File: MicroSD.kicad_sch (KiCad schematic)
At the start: 9 parts, among them J1 Micro_SD_Card_Det1

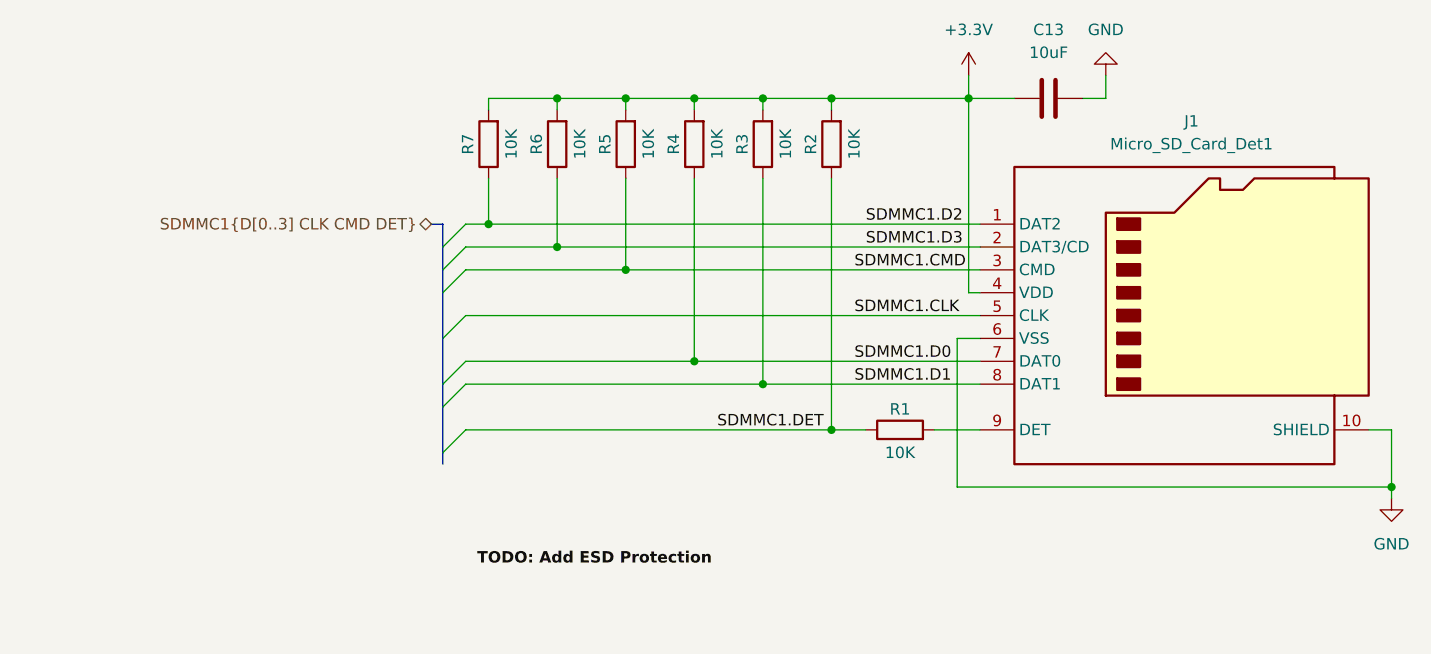
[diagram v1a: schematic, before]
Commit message: FIX : uSD Card detect
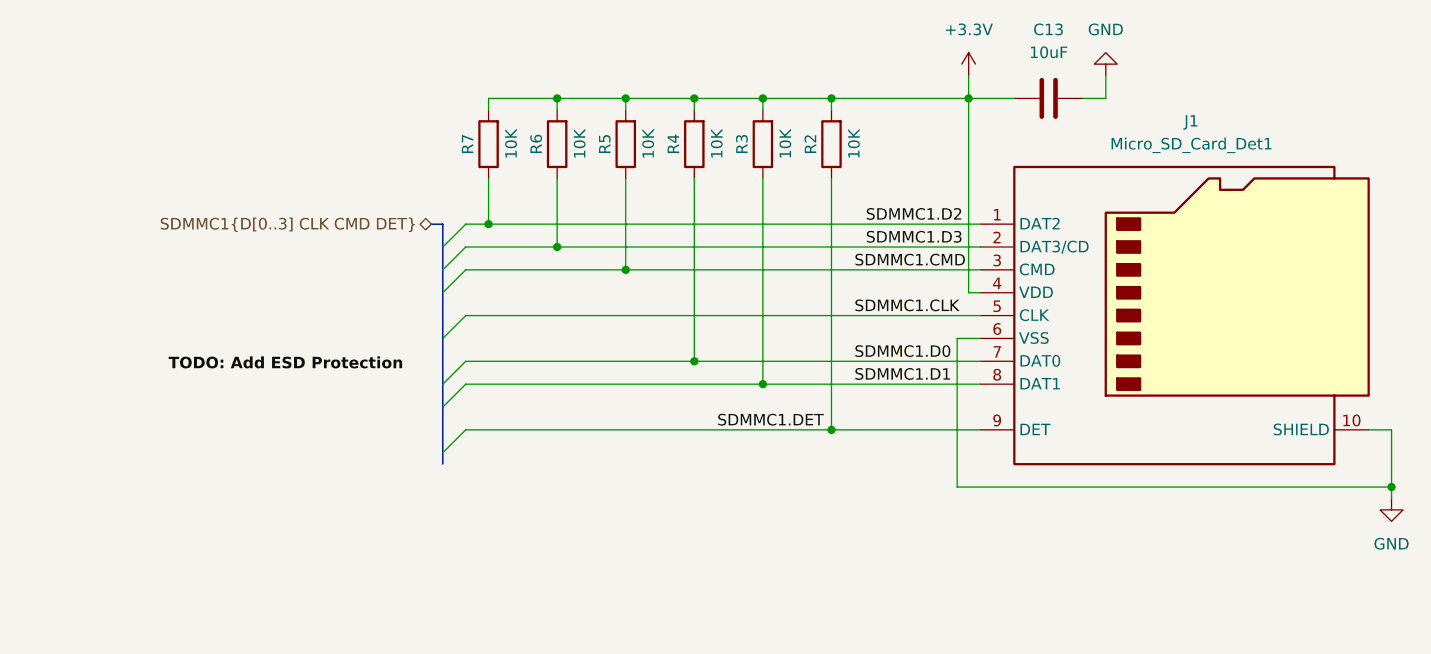
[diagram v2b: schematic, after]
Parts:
- removed R1: 10K, symbol Device:R
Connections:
- net SDMMC1.DET: now also J1.9 (DET)
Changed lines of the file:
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@@
 	(wire
 		(pts
-			(xy 105.41 109.22) (xy 109.22 109.22)
+			(xy 105.41 109.22) (xy 121.92 109.22)
 		)
 		(stroke
@@
 		(pts
 			(xy 67.31 86.36) (xy 121.92 86.36)
-		)
-		(stroke
-			(width 0)
-			(type default)
-		)
-	)
-	(wire
-		(pts
-			(xy 116.84 109.22) (xy 121.92 109.22)
 		)
 		(stroke
@@
 	)
 	(label "TODO: Add ESD Protection"
-		(at 66.04 124.46 0)
+		(at 31.75 102.87 0)
 		(effects
 			(font
@@
 					(unit 1)
 				)
-			)
-		)
-	)
-	(symbol
-		(lib_id "Device:R")
-		(at 113.03 109.22 90)
-		(unit 1)
-		(exclude_from_sim no)
-		(in_bom yes)
-		(on_board yes)
-		(dnp no)
-		(property "Reference" "R1"
-			(at 113.03 106.934 90)
-			(effects
-				(font
-					(size 1.27 1.27)
-				)
-			)
-		)
-		(property "Value" "10K"
-			(at 113.03 111.76 90)
-			(effects
-				(font
-					(size 1.27 1.27)
-				)
-			)
-		)
-		(property "Footprint" ""
-			(at 113.03 110.998 90)
-			(effects
-				(font
-					(size 1.27 1.27)
-				)
-				(hide yes)
-			)
-		)
-		(property "Datasheet" "~"
-			(at 113.03 109.22 0)
-			(effects
-				(font
-					(size 1.27 1.27)
-				)
-				(hide yes)
-			)
-		)
-		(property "Description" "Resistor"
-			(at 113.03 109.22 0)
-			(effects
-				(font
-					(size 1.27 1.27)
-				)
-				(hide yes)
-			)
-		)
-		(pin "2"
-		)
-		(pin "1"
-		)
-		(instances
-			(project "STMBlueLine"
-				(path "/d9f70aa0-fcfd-4ae4-9801-1024ce5b770a/b1a92380-38d8-44e8-bc23-33aa2ab32880"
-					(reference "R1")
-					(unit 1)
-				)

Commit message: ADD : ESD protection for uSD. FIX : uSD pullups
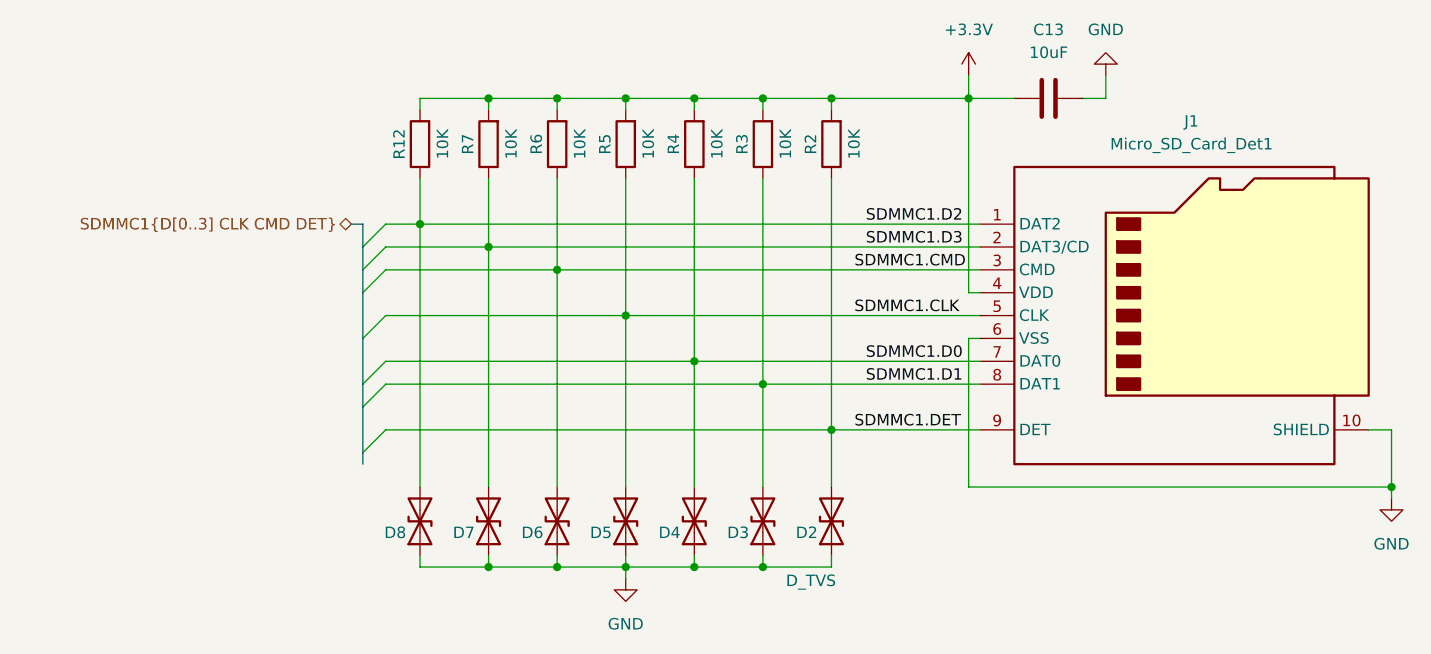
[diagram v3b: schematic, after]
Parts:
- added D2, D3, D4, D5, D6, D7, D8: D_TVS, symbol Device:D_TVS
- added R12: 10K, symbol Device:R
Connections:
- net +3.3V: now also R12.2
- net GND: now also D2.1 (A1), D3.1 (A1), D4.1 (A1), D5.1 (A1), D6.1 (A1), D7.1 (A1), D8.1 (A1)
- net SDMMC1.CLK: now also R5.1, D5.2 (A2)
- net SDMMC1.CMD: now also R6.1, D6.2 (A2); no longer R5.1
- net SDMMC1.D0: now also D4.2 (A2)
- net SDMMC1.D1: now also D3.2 (A2)
- net SDMMC1.D2: now also D8.2 (A2), R12.1; no longer R7.1
- net SDMMC1.D3: now also R7.1, D7.2 (A2); no longer R6.1
- net SDMMC1.DET: now also D2.2 (A2)

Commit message: ADD : Footprint assignment. FIX : Various ERC rules.
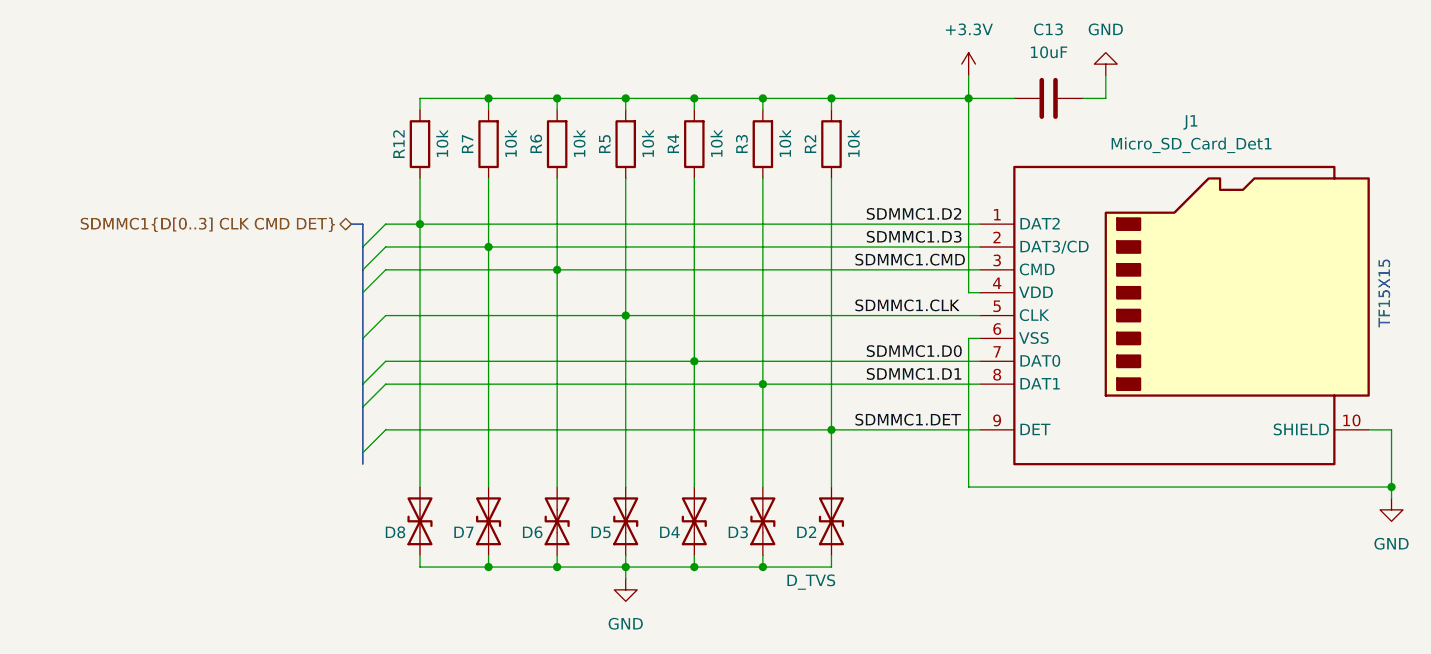
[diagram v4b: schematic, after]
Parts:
- C13: footprint (none) -> Capacitor_SMD:C_0402_1005Metric
- D2, D3, D4, D5, D6, D7, D8: footprint (none) -> Diode_SMD:D_0402_1005Metric
- J1: footprint (none) -> random-footprints:TF15X15
- R12, R2, R3, R4, R5, R6, R7: value 10K -> 10k; footprint (none) -> Resistor_SMD:R_0402_1005Metric
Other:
- note added: "TF15X15"
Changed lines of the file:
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@@
 	(generator_version "9.0")
 	(paper "A4")
+	(text "TF15X15"
+		(exclude_from_sim no)
+		(at 166.878 94.234 90)
+		(effects
+			(font
+				(size 1.27 1.27)
+			)
+		)
+	)
 	(junction
 		(at 97.79 124.46)
@@
 			)
 		)
-		(property "Value" "10K"
+		(property "Value" "10k"
 			(at 77.47 77.47 90)
 			(effects
@@
 			)
 		)
-		(property "Footprint" ""
+		(property "Footprint" "Resistor_SMD:R_0402_1005Metric"
 			(at 76.708 77.47 90)
 			(effects
@@
 			)
 		)
-		(property "Value" "10K"
+		(property "Value" "10k"
 			(at 85.09 77.47 90)
 			(effects
@@
 			)
 		)
-		(property "Footprint" ""
+		(property "Footprint" "Resistor_SMD:R_0402_1005Metric"
 			(at 84.328 77.47 90)
 			(effects
@@
 			)
 		)
-		(property "Value" "10K"
+		(property "Value" "10k"
 			(at 62.23 77.47 90)
 			(effects
@@
 			)
 		)
-		(property "Footprint" ""
+		(property "Footprint" "Resistor_SMD:R_0402_1005Metric"
 			(at 61.468 77.47 90)
 			(effects
@@
 			)
 		)
-		(property "Footprint" ""
+		(property "Footprint" "random-footprints:TF15X15"
 			(at 196.85 78.74 0)
 			(effects
@@
 			)
 		)
-		(property "Footprint" ""
+		(property "Footprint" "Diode_SMD:D_0402_1005Metric"
 			(at 105.41 119.38 0)
 			(effects
@@
 			)
 		)
-		(property "Value" "10K"
+		(property "Value" "10k"
 			(at 107.95 77.47 90)
 			(effects
@@
 			)
 		)
-		(property "Footprint" ""
+		(property "Footprint" "Resistor_SMD:R_0402_1005Metric"
 			(at 107.188 77.47 90)
 			(effects
@@
 			)
 		)
-		(property "Value" "10K"
+		(property "Value" "10k"
 			(at 69.85 77.47 90)
 			(effects
@@
 			)
 		)
-		(property "Footprint" ""
+		(property "Footprint" "Resistor_SMD:R_0402_1005Metric"
 			(at 69.088 77.47 90)
 			(effects
@@
 			)
 		)
-		(property "Footprint" ""
+		(property "Footprint" "Diode_SMD:D_0402_1005Metric"
 			(at 90.17 119.38 0)
 			(effects
@@
 			)
 		)
-		(property "Footprint" ""
+		(property "Footprint" "Diode_SMD:D_0402_1005Metric"
 			(at 59.69 119.38 0)
 			(effects
@@
 			)
 		)
-		(property "Footprint" ""
+		(property "Footprint" "Diode_SMD:D_0402_1005Metric"
 			(at 97.79 119.38 0)
 			(effects
@@
 			)
 		)
-		(property "Footprint" ""
+		(property "Footprint" "Diode_SMD:D_0402_1005Metric"
 			(at 74.93 119.38 0)
 			(effects
@@
 			)
 		)
-		(property "Value" "10K"
+		(property "Value" "10k"
 			(at 92.71 77.47 90)
 			(effects
@@
 			)
 		)
-		(property "Footprint" ""
+		(property "Footprint" "Resistor_SMD:R_0402_1005Metric"
 			(at 91.948 77.47 90)
 			(effects
@@
 			)
 		)
-		(property "Footprint" ""
+		(property "Footprint" "Diode_SMD:D_0402_1005Metric"
 			(at 82.55 119.38 0)
 			(effects
@@
 			)
 		)
-		(property "Footprint" ""
+		(property "Footprint" "Diode_SMD:D_0402_1005Metric"
 			(at 67.31 119.38 0)
 			(effects
@@
 			)
 		)
-		(property "Value" "10K"
+		(property "Value" "10k"
 			(at 100.33 77.47 90)
 			(effects
@@
 			)
 		)
-		(property "Footprint" ""
+		(property "Footprint" "Resistor_SMD:R_0402_1005Metric"
 			(at 99.568 77.47 90)
 			(effects
@@
 			)
 		)
-		(property "Footprint" ""
+		(property "Footprint" "Capacitor_SMD:C_0402_1005Metric"
 			(at 133.35 71.4248 0)
 			(effects

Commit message: ADD : Rough PCB part placement. MOD : Swapped codec DVDD LDO.
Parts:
- J1: footprint random-footprints:TF15X15 -> easyeda2kicad:TF-SMD_TF-123-ARP9H15
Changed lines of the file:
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@@
 			)
 		)
-		(property "Footprint" "random-footprints:TF15X15"
+		(property "Footprint" "easyeda2kicad:TF-SMD_TF-123-ARP9H15"
 			(at 196.85 78.74 0)
 			(effects
